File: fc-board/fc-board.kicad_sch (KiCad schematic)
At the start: 35 parts, among them J1 M80-5000442, J10 BCS-110-L-D-TE, J11 Conn_Coaxial_Small, J12 Conn_01x03_Pin, J13 RJMG201K32630ER, J2 M80-5000442, J3 M80-5000442, J4 M80-5000442, J5 M80-5000442, J6 Conn_02x04_Counter_Clockwise, J7 Conn_02x02_Counter_Clockwise, J8 Conn_01x08_Pin, J9 Conn_01x02_Pin

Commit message: Updated RJ45 jack
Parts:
- removed C1, C2: 0.1u, Capacitor_SMD:C_0805_2012Metric, symbol Device:C_Small
- removed J13: RJMG201K32630ER, fc-board:RJMG201K32630ER, symbol fc-board:RJMG201K32630ER
- removed JP2: SHIELD, Resistor_SMD:R_1206_3216Metric_Pad1.30x1.75mm_HandSolder, symbol Jumper:SolderJumper_2_Open
- added JP2: 74981104402, fc-board:74981104402, symbol fc-board:74981104402
- JP3: value SHIELD1 -> CHASSIS_GND; footprint Resistor_SMD:R_1206_3216Metric_Pad1.30x1.75mm_HandSolder -> Jumper:SolderJumper-2_P1.3mm_Open_Pad1.0x1.5mm
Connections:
- net GND: now also JP2.1 (GND)
- net Y1+: now also JP2.2 (D1+)
- net Y1-: now also JP2.3 (D1-)
- net Y2+: now also JP2.4 (D2+)
- net Y2-: now also JP2.5 (D2-)
- net Y3+: now also JP2.6 (D3+)
- net Y3-: now also JP2.7 (D3-)
- net Y4+: now also JP2.8 (D4+)
- net Y4-: now also JP2.9 (D4-)
- net Y_DUPLEX_LED: now also JP2.14
- net Y_LINK_LED: now also JP2.12
- net at R3.2: now also JP2.13
- net CHASSIS: now reaches JP3.1 (A)
- net CHASSIS: now also JP2.S1 (SHIELD1), JP2.S2 (SHIELD2)
- net at R2.2: now also JP2.11
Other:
- note added: "CHASSIS!!! CHANGE THIS"
- note added: "CONNECT THESE TO CHASSIS WHEN BOARD REWORKED"
- note removed: "Jumpers for connecting shield to GND with either resistor or capacitor"
- note removed: "The LAN7430 PCIE card shows capacitors connecting the center taps to GND"
- note removed: "Unsure if the LEDs are properly labeled on the symbol; don't have a part in house to check atm."
- moved on the sheet: R2, R3

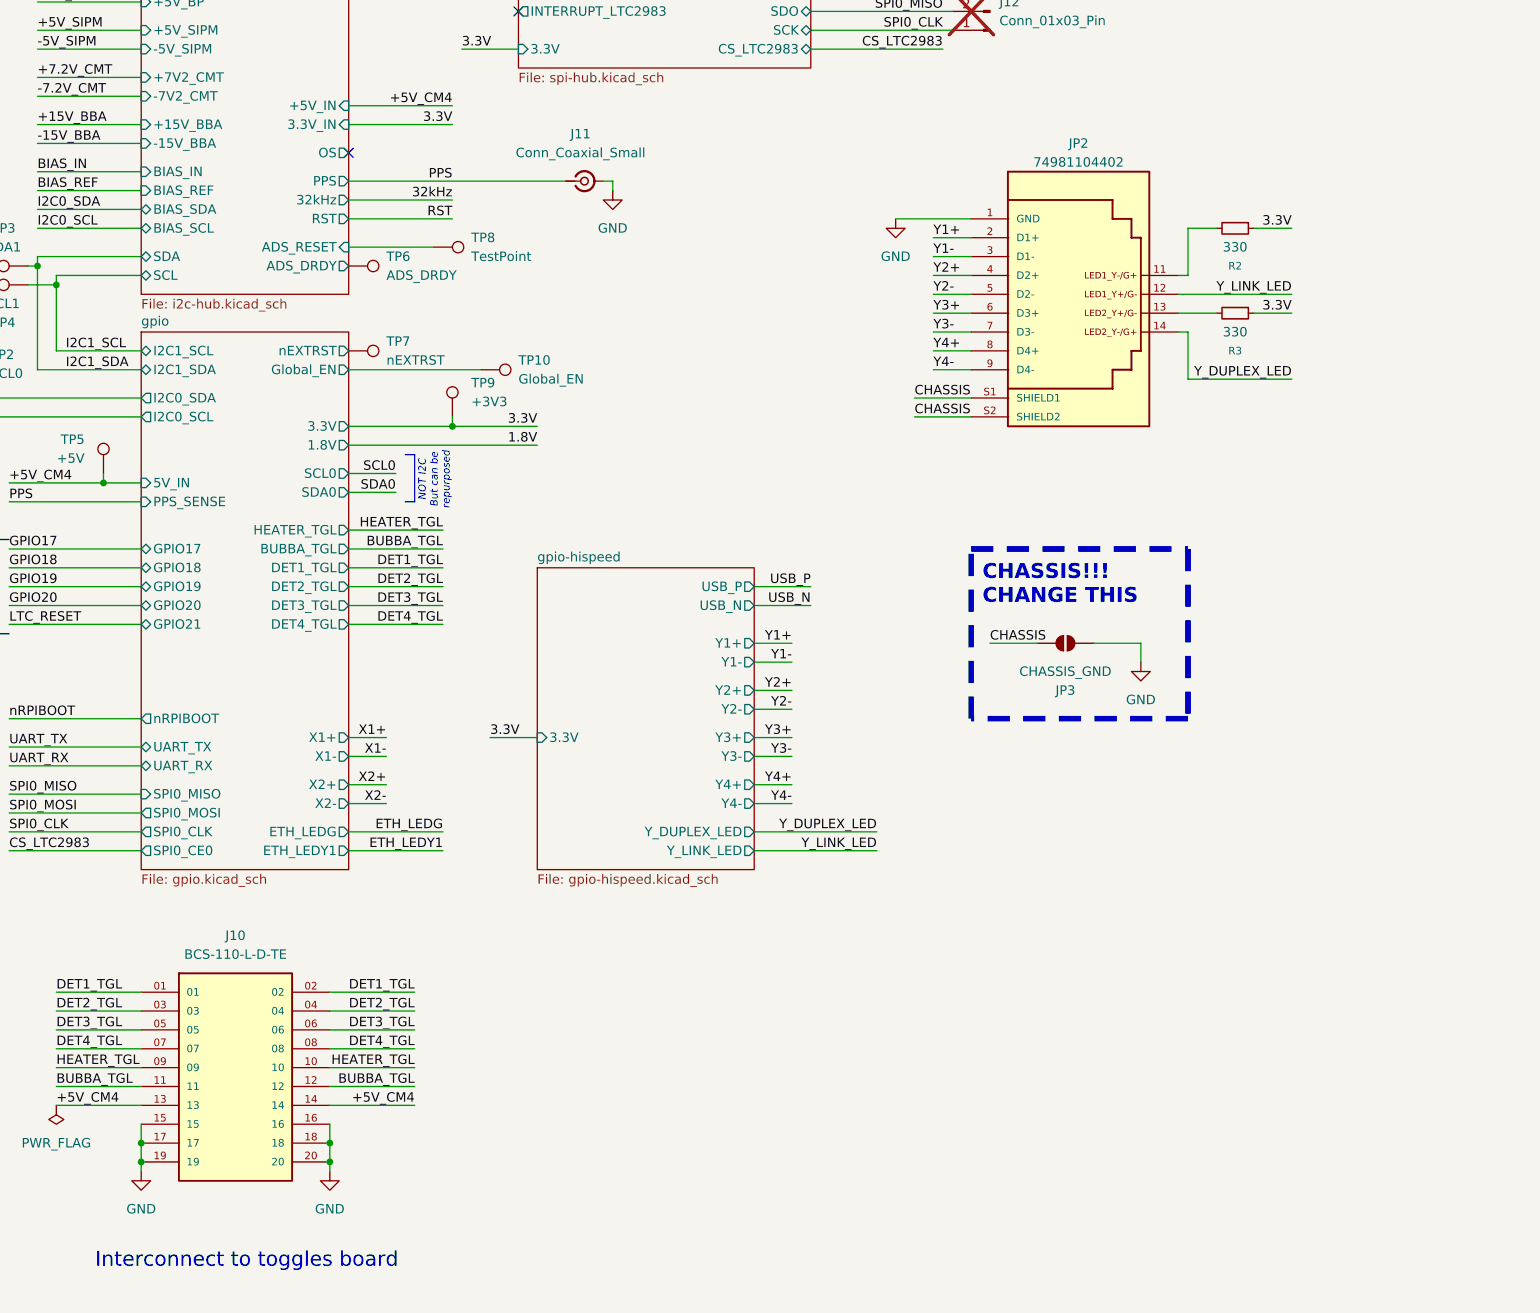
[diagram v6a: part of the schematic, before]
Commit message: Assigned part numbers to everything, replaced ethernet jack
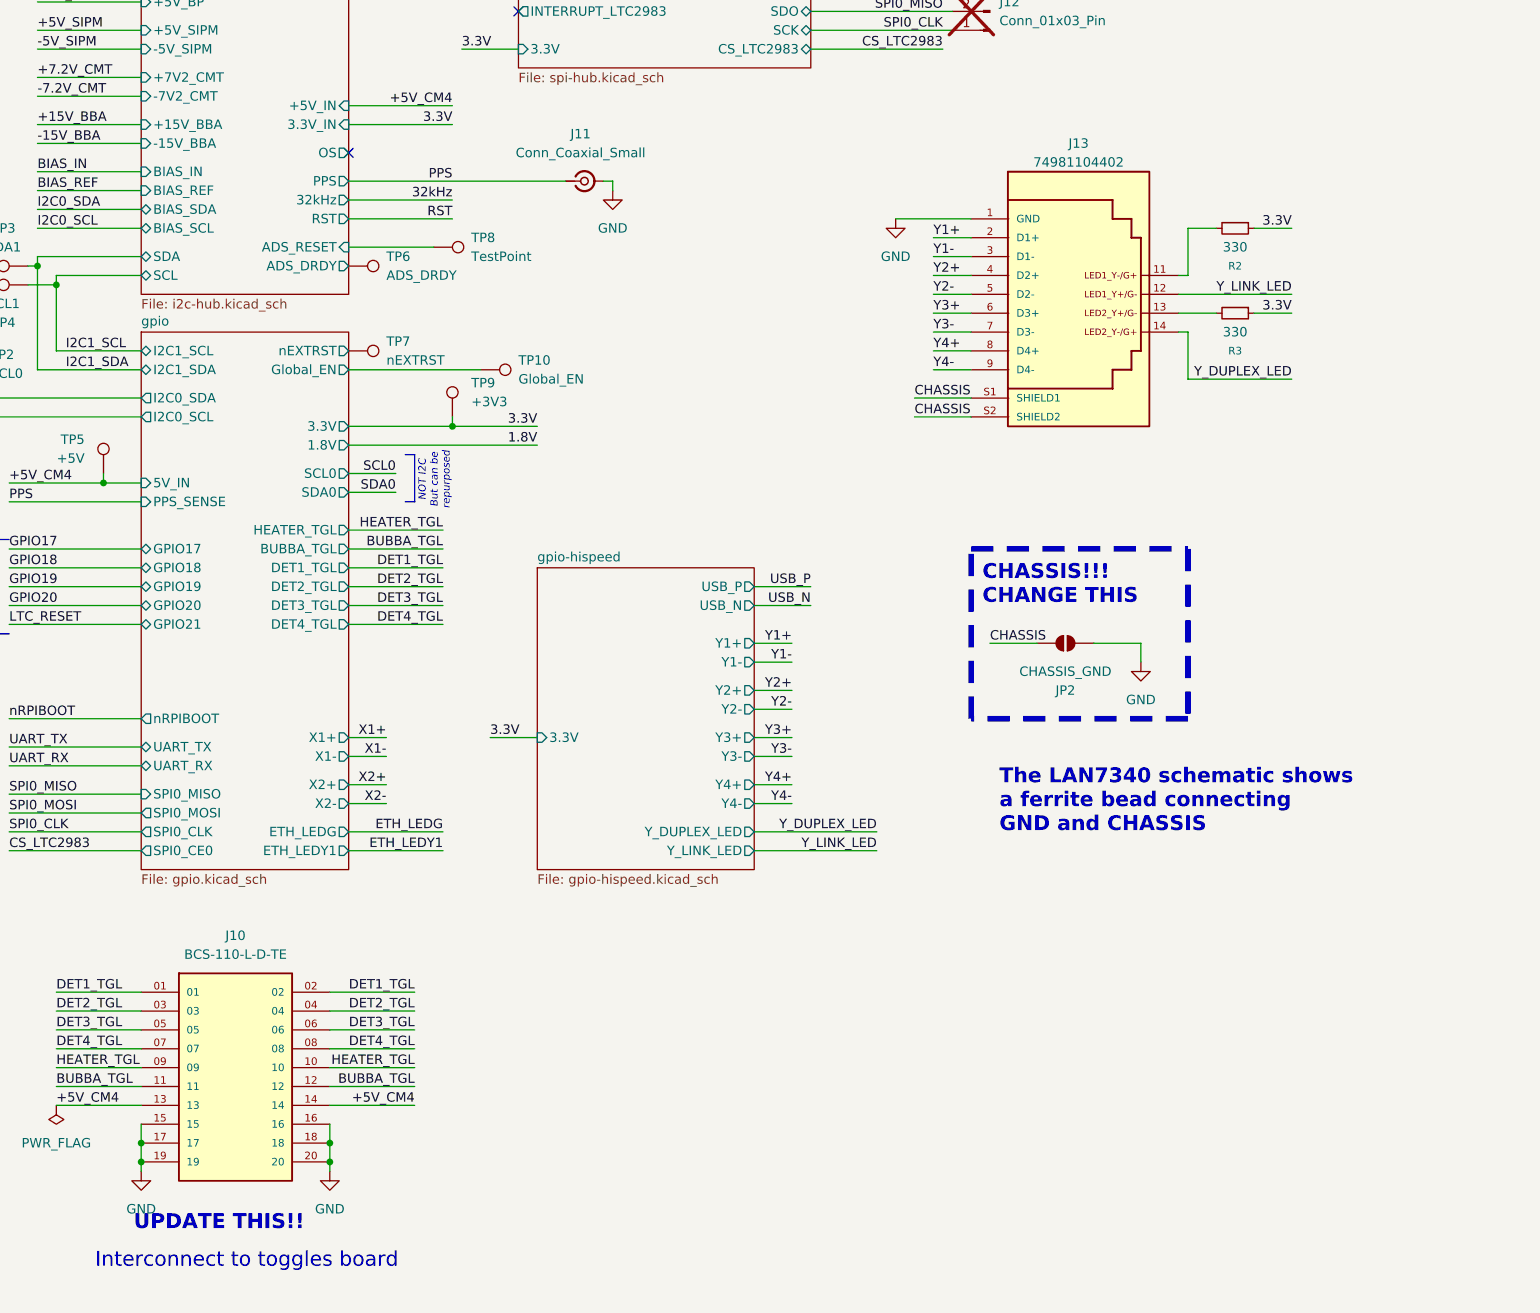
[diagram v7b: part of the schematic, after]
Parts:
- renumbered JP2 to J13, JP3 to JP2
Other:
- note added: "The LAN7340 schematic shows a ferrite bead connecting GND and CHASSIS"
- note added: "UPDATE THIS!!"

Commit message: Finalized layout
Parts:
- removed J10: BCS-110-L-D-TE, fc-board:SAMTEC_BCS-110-L-D-TE, symbol fc-board:BCS-110-L-D-TE
- added J10: MTSW-110-13-L-D-1060, fc-board:SAMTEC_BCS-110-L-D-TE, symbol Connector_Generic:Conn_02x10_Odd_Even
- J6: value Conn_02x04_Counter_Clockwise -> MTSW-104-13-L-D-1060
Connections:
- net +5V_CM4: now also J10.13 (Pin_13), J10.14 (Pin_14)
- net BUBBA_TGL: now also J10.11 (Pin_11), J10.12 (Pin_12)
- net DET1_TGL: now also J10.1 (Pin_1), J10.2 (Pin_2)
- net DET2_TGL: now also J10.3 (Pin_3), J10.4 (Pin_4)
- net DET3_TGL: now also J10.5 (Pin_5), J10.6 (Pin_6)
- net DET4_TGL: now also J10.7 (Pin_7), J10.8 (Pin_8)
- net GND: now also J10.15 (Pin_15), J10.16 (Pin_16), J10.17 (Pin_17), J10.18 (Pin_18), J10.19 (Pin_19), J10.20 (Pin_20)
- net HEATER_TGL: now also J10.10 (Pin_10), J10.9 (Pin_9)
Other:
- note removed: "UPDATE THIS!!"
